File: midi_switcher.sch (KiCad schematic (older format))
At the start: 0 parts

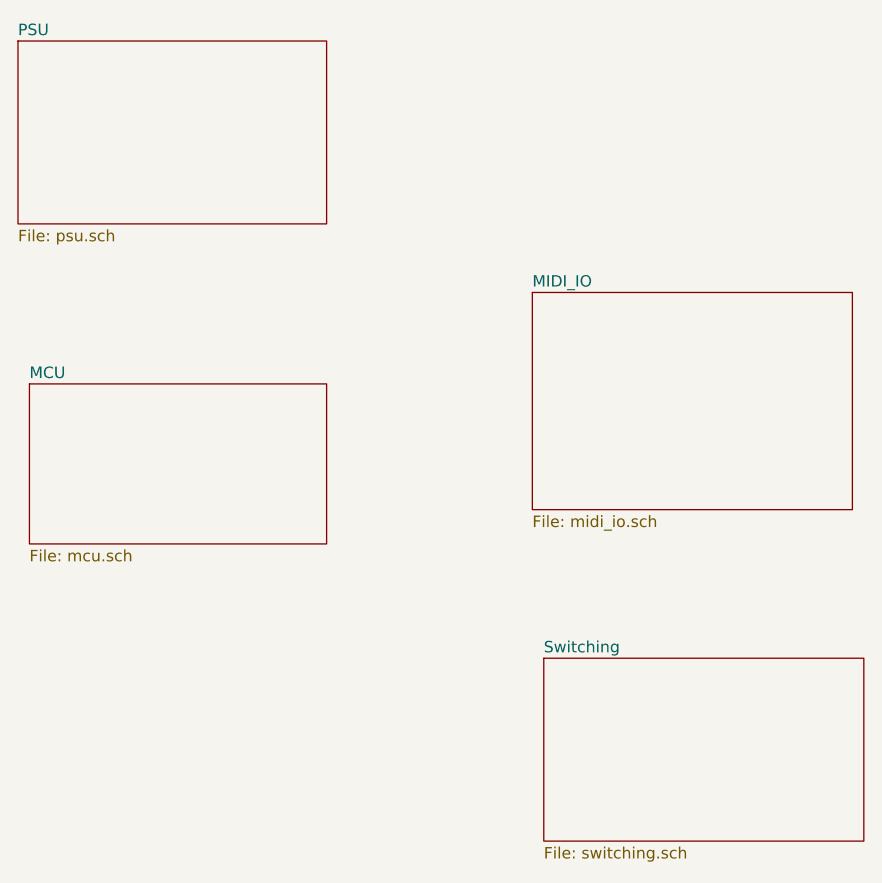
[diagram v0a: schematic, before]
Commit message: Schem entry done, need to do footprints and PCB
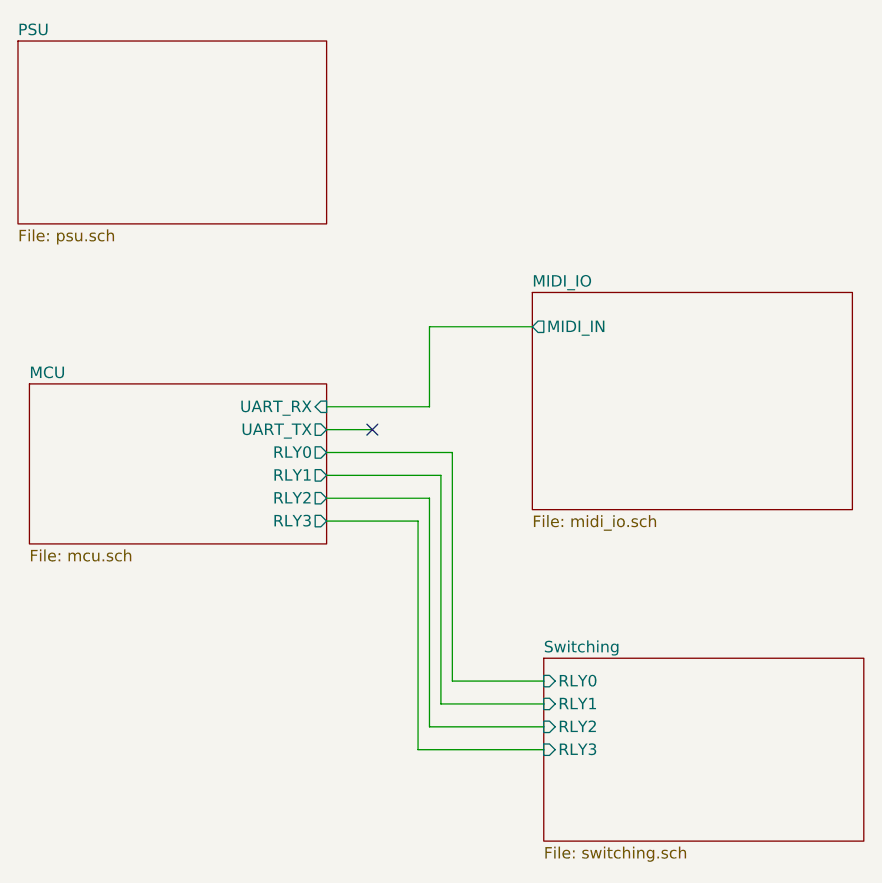
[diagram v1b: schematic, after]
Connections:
- no-connect marks 0 -> 1
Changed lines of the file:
@@
 EESchema Schematic File Version 4
 LIBS:midi_switcher-cache
-EELAYER 29 0
+EELAYER 30 0
 EELAYER END
 $Descr A4 11693 8268
@@
 F0 "MCU" 50
 F1 "mcu.sch" 50
+F2 "UART_RX" I R 3000 2750 50
+F3 "UART_TX" O R 3000 2850 50
+F4 "RLY0" O R 3000 2950 50
+F5 "RLY1" O R 3000 3050 50
+F6 "RLY2" O R 3000 3150 50
+F7 "RLY3" O R 3000 3250 50
 $EndSheet
 $Sheet
@@
 F0 "MIDI_IO" 50
 F1 "midi_io.sch" 50
+F2 "MIDI_IN" O L 3900 2400 50
 $EndSheet
 $Sheet
@@
 F0 "Switching" 50
 F1 "switching.sch" 50
+F2 "RLY0" I L 3950 3950 50
+F3 "RLY1" I L 3950 4050 50
+F4 "RLY2" I L 3950 4150 50
+F5 "RLY3" I L 3950 4250 50
 $EndSheet
+Wire Wire Line
+	3000 2750 3450 2750
+Wire Wire Line
+	3450 2750 3450 2400
+Wire Wire Line
+	3450 2400 3900 2400
+Wire Wire Line
+	3000 2850 3200 2850
+NoConn ~ 3200 2850
+Wire Wire Line
+	3000 2950 3550 2950
+Wire Wire Line
+	3550 2950 3550 3950
+Wire Wire Line
+	3550 3950 3950 3950
+Wire Wire Line
+	3000 3050 3500 3050
+Wire Wire Line
+	3500 3050 3500 4050
+Wire Wire Line
+	3500 4050 3950 4050
+Wire Wire Line
+	3000 3150 3450 3150
+Wire Wire Line
+	3450 3150 3450 4150
+Wire Wire Line
+	3450 4150 3950 4150
+Wire Wire Line
+	3000 3250 3400 3250
+Wire Wire Line
+	3400 3250 3400 4250
+Wire Wire Line
+	3400 4250 3950 4250
 $EndSCHEMATC
